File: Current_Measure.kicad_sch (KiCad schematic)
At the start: 4 parts, among them U9401 TMCS1101A2UQDT

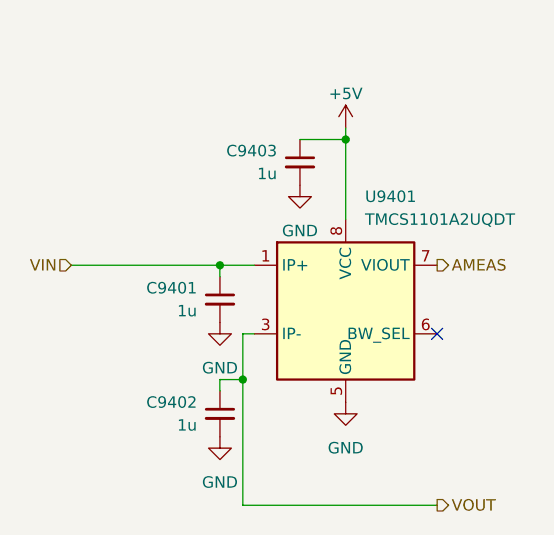
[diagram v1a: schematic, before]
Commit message: wired channel alerts; added schematic for test pbc
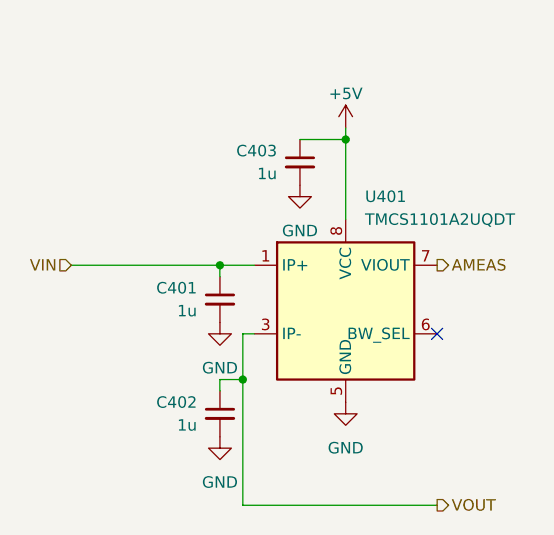
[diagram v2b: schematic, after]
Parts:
- renumbered C9401 to C401, C9402 to C402, C9403 to C403, U9401 to U401
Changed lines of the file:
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@@
 		(on_board yes)
 		(dnp no)
-		(property "Reference" "#PWR09404"
+		(property "Reference" "#PWR0404"
 			(at 157.48 77.47 0)
 			(effects
@@
 		)
 		(instances
+			(project "TEST_PCB"
+				(path "/29496ace-b476-4f24-a65f-9da1dd70122c/504ee284-c5b3-48b9-b988-a6d19662e437"
+					(reference "#PWR01304")
+					(unit 1)
+				)
+				(path "/29496ace-b476-4f24-a65f-9da1dd70122c/02ad1486-0ecd-4655-9f01-754da17b7441/24296571-f4ee-420c-bcfd-9dd9216b9bef"
+					(reference "#PWR0404")
+					(unit 1)
+				)
+			)
 			(project "EPS"
 				(path "/94201994-47b8-4213-8d1a-05da12b2a7b0/48aa2731-b960-4e20-aa69-ef710a76283c"
@@
 		(dnp no)
 		(fields_autoplaced yes)
-		(property "Reference" "#PWR09402"
+		(property "Reference" "#PWR0402"
 			(at 143.51 114.3 0)
 			(effects
@@
 		)
 		(instances
+			(project "TEST_PCB"
+				(path "/29496ace-b476-4f24-a65f-9da1dd70122c/504ee284-c5b3-48b9-b988-a6d19662e437"
+					(reference "#PWR01302")
+					(unit 1)
+				)
+				(path "/29496ace-b476-4f24-a65f-9da1dd70122c/02ad1486-0ecd-4655-9f01-754da17b7441/24296571-f4ee-420c-bcfd-9dd9216b9bef"
+					(reference "#PWR0402")
+					(unit 1)
+				)
+			)
 			(project "EPS"
 				(path "/94201994-47b8-4213-8d1a-05da12b2a7b0/48aa2731-b960-4e20-aa69-ef710a76283c"
@@
 		(on_board yes)
 		(dnp no)
-		(property "Reference" "C9401"
+		(property "Reference" "C401"
 			(at 140.97 91.4462 0)
 			(effects
@@
 		)
 		(instances
+			(project "TEST_PCB"
+				(path "/29496ace-b476-4f24-a65f-9da1dd70122c/504ee284-c5b3-48b9-b988-a6d19662e437"
+					(reference "C1301")
+					(unit 1)
+				)
+				(path "/29496ace-b476-4f24-a65f-9da1dd70122c/02ad1486-0ecd-4655-9f01-754da17b7441/24296571-f4ee-420c-bcfd-9dd9216b9bef"
+					(reference "C401")
+					(unit 1)
+				)
+			)
 			(project "EPS"
 				(path "/94201994-47b8-4213-8d1a-05da12b2a7b0/48aa2731-b960-4e20-aa69-ef710a76283c"
@@
 		(dnp no)
 		(fields_autoplaced yes)
-		(property "Reference" "#PWR09405"
+		(property "Reference" "#PWR0405"
 			(at 157.48 110.49 0)
 			(effects
@@
 		)
 		(instances
+			(project "TEST_PCB"
+				(path "/29496ace-b476-4f24-a65f-9da1dd70122c/504ee284-c5b3-48b9-b988-a6d19662e437"
+					(reference "#PWR01305")
+					(unit 1)
+				)
+				(path "/29496ace-b476-4f24-a65f-9da1dd70122c/02ad1486-0ecd-4655-9f01-754da17b7441/24296571-f4ee-420c-bcfd-9dd9216b9bef"
+					(reference "#PWR0405")
+					(unit 1)
+				)
+			)
 			(project "EPS"
 				(path "/94201994-47b8-4213-8d1a-05da12b2a7b0/48aa2731-b960-4e20-aa69-ef710a76283c"
@@
 		(dnp no)
 		(fields_autoplaced yes)
-		(property "Reference" "U9401"
+		(property "Reference" "U401"
 			(at 159.6233 81.28 0)
 			(effects
@@
 		)
 		(instances
+			(project "TEST_PCB"
+				(path "/29496ace-b476-4f24-a65f-9da1dd70122c/504ee284-c5b3-48b9-b988-a6d19662e437"
+					(reference "U1301")
+					(unit 1)
+				)
+				(path "/29496ace-b476-4f24-a65f-9da1dd70122c/02ad1486-0ecd-4655-9f01-754da17b7441/24296571-f4ee-420c-bcfd-9dd9216b9bef"
+					(reference "U401")
+					(unit 1)
+				)
+			)
 			(project "EPS"
 				(path "/94201994-47b8-4213-8d1a-05da12b2a7b0/48aa2731-b960-4e20-aa69-ef710a76283c"
@@
 		(on_board yes)
 		(dnp no)
-		(property "Reference" "C9403"
+		(property "Reference" "C403"
 			(at 149.86 76.2062 0)
 			(effects
@@
 		)
 		(instances
+			(project "TEST_PCB"
+				(path "/29496ace-b476-4f24-a65f-9da1dd70122c/504ee284-c5b3-48b9-b988-a6d19662e437"
+					(reference "C1303")
+					(unit 1)
+				)
+				(path "/29496ace-b476-4f24-a65f-9da1dd70122c/02ad1486-0ecd-4655-9f01-754da17b7441/24296571-f4ee-420c-bcfd-9dd9216b9bef"
+					(reference "C403")
+					(unit 1)
+				)
+			)
 			(project "EPS"
 				(path "/94201994-47b8-4213-8d1a-05da12b2a7b0/48aa2731-b960-4e20-aa69-ef710a76283c"
@@
 		(on_board yes)
 		(dnp no)
-		(property "Reference" "C9402"
+		(property "Reference" "C402"
 			(at 140.97 104.1462 0)
 			(effects
@@
 		)
 		(instances
+			(project "TEST_PCB"
+				(path "/29496ace-b476-4f24-a65f-9da1dd70122c/504ee284-c5b3-48b9-b988-a6d19662e437"
+					(reference "C1302")
+					(unit 1)
+				)
+				(path "/29496ace-b476-4f24-a65f-9da1dd70122c/02ad1486-0ecd-4655-9f01-754da17b7441/24296571-f4ee-420c-bcfd-9dd9216b9bef"
+					(reference "C402")
+					(unit 1)
+				)
+			)
 			(project "EPS"
 				(path "/94201994-47b8-4213-8d1a-05da12b2a7b0/48aa2731-b960-4e20-aa69-ef710a76283c"
@@
 		(dnp no)
 		(fields_autoplaced yes)
-		(property "Reference" "#PWR09401"
+		(property "Reference" "#PWR0401"
 			(at 143.51 101.6 0)
 			(effects
@@
 		)
 		(instances
+			(project "TEST_PCB"
+				(path "/29496ace-b476-4f24-a65f-9da1dd70122c/504ee284-c5b3-48b9-b988-a6d19662e437"
+					(reference "#PWR01301")
+					(unit 1)
+				)
+				(path "/29496ace-b476-4f24-a65f-9da1dd70122c/02ad1486-0ecd-4655-9f01-754da17b7441/24296571-f4ee-420c-bcfd-9dd9216b9bef"
+					(reference "#PWR0401")
+					(unit 1)
+				)
+			)
 			(project "EPS"
 				(path "/94201994-47b8-4213-8d1a-05da12b2a7b0/48aa2731-b960-4e20-aa69-ef710a76283c"
@@
 		(dnp no)
 		(fields_autoplaced yes)
-		(property "Reference" "#PWR09403"
+		(property "Reference" "#PWR0403"
 			(at 152.4 86.36 0)
 			(effects
@@
 		)
 		(instances
+			(project "TEST_PCB"
+				(path "/29496ace-b476-4f24-a65f-9da1dd70122c/504ee284-c5b3-48b9-b988-a6d19662e437"
+					(reference "#PWR01303")
+					(unit 1)
+				)
+				(path "/29496ace-b476-4f24-a65f-9da1dd70122c/02ad1486-0ecd-4655-9f01-754da17b7441/24296571-f4ee-420c-bcfd-9dd9216b9bef"
+					(reference "#PWR0403")
+					(unit 1)
+				)
+			)
 			(project "EPS"
 				(path "/94201994-47b8-4213-8d1a-05da12b2a7b0/48aa2731-b960-4e20-aa69-ef710a76283c"

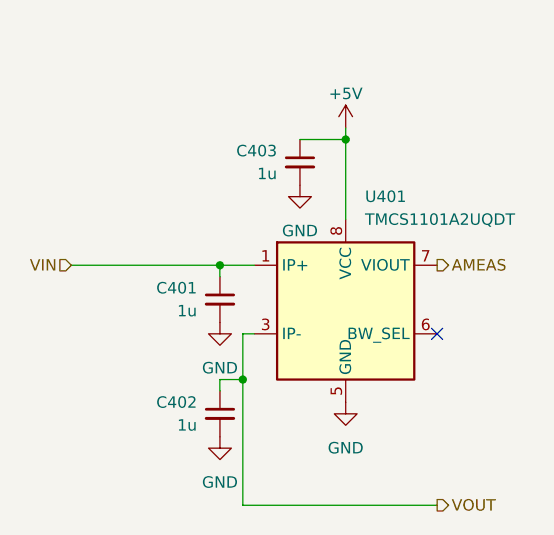
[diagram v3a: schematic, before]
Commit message: added missing heater connectors
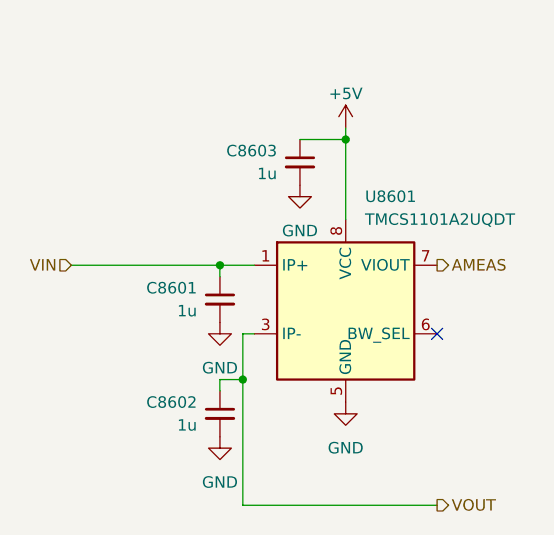
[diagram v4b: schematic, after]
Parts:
- renumbered C401 to C8601, C402 to C8602, C403 to C8603, U401 to U8601
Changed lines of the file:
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@@
 		(on_board yes)
 		(dnp no)
-		(property "Reference" "#PWR0404"
+		(property "Reference" "#PWR08604"
 			(at 157.48 77.47 0)
 			(effects
@@
 		(dnp no)
 		(fields_autoplaced yes)
-		(property "Reference" "#PWR0402"
+		(property "Reference" "#PWR08602"
 			(at 143.51 114.3 0)
 			(effects
@@
 		(on_board yes)
 		(dnp no)
-		(property "Reference" "C401"
+		(property "Reference" "C8601"
 			(at 140.97 91.4462 0)
 			(effects
@@
 		(dnp no)
 		(fields_autoplaced yes)
-		(property "Reference" "#PWR0405"
+		(property "Reference" "#PWR08605"
 			(at 157.48 110.49 0)
 			(effects
@@
 		(dnp no)
 		(fields_autoplaced yes)
-		(property "Reference" "U401"
+		(property "Reference" "U8601"
 			(at 159.6233 81.28 0)
 			(effects
@@
 		(on_board yes)
 		(dnp no)
-		(property "Reference" "C403"
+		(property "Reference" "C8603"
 			(at 149.86 76.2062 0)
 			(effects
@@
 		(on_board yes)
 		(dnp no)
-		(property "Reference" "C402"
+		(property "Reference" "C8602"
 			(at 140.97 104.1462 0)
 			(effects
@@
 		(dnp no)
 		(fields_autoplaced yes)
-		(property "Reference" "#PWR0401"
+		(property "Reference" "#PWR08601"
 			(at 143.51 101.6 0)
 			(effects
@@
 		(dnp no)
 		(fields_autoplaced yes)
-		(property "Reference" "#PWR0403"
+		(property "Reference" "#PWR08603"
 			(at 152.4 86.36 0)
 			(effects

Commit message: restructurization of the entire project improved
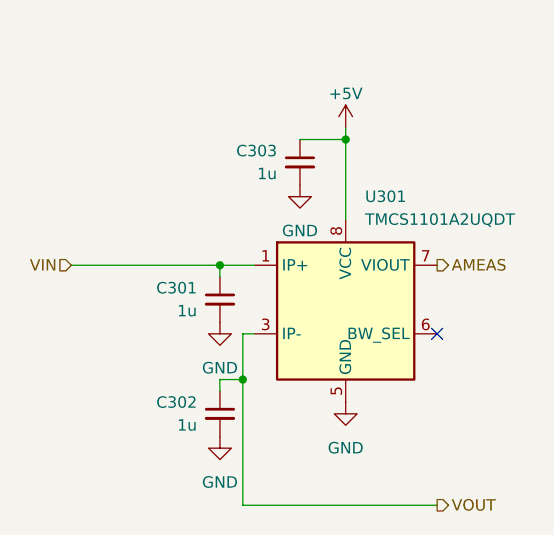
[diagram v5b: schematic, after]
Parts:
- renumbered C8601 to C301, C8602 to C302, C8603 to C303, U8601 to U301

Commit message: added universal switch, added simples current source, reworked test schematic and pcb
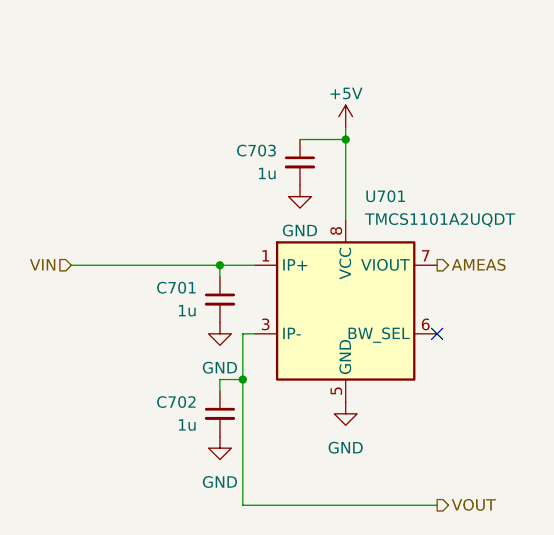
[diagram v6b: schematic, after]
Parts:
- renumbered C301 to C701, C302 to C702, C303 to C703, U301 to U701
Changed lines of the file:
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@@
 		(on_board yes)
 		(dnp no)
-		(property "Reference" "#PWR0304"
+		(property "Reference" "#PWR0704"
 			(at 157.48 77.47 0)
 			(effects
@@
 		)
 		(instances
+			(project "TEST_PCB"
+				(path "/29496ace-b476-4f24-a65f-9da1dd70122c/504ee284-c5b3-48b9-b988-a6d19662e437"
+					(reference "#PWR01404")
+					(unit 1)
+				)
+				(path "/29496ace-b476-4f24-a65f-9da1dd70122c/9ac70773-2304-4605-b1e0-d7d1b5f027ba"
+					(reference "#PWR0704")
+					(unit 1)
+				)
+				(path "/29496ace-b476-4f24-a65f-9da1dd70122c/02ad1486-0ecd-4655-9f01-754da17b7441/24296571-f4ee-420c-bcfd-9dd9216b9bef"
+					(reference "#PWR01604")
+					(unit 1)
+				)
+			)
 			(project "EPS_CORE"
 				(path "/43e5e7c8-e7e0-4528-9a3e-b1557849918d/136d551b-dd5b-42cc-aebd-902cdeeb5d77"
@@
 		(dnp no)
 		(fields_autoplaced yes)
-		(property "Reference" "#PWR0302"
+		(property "Reference" "#PWR0702"
 			(at 143.51 114.3 0)
 			(effects
@@
 		)
 		(instances
+			(project "TEST_PCB"
+				(path "/29496ace-b476-4f24-a65f-9da1dd70122c/504ee284-c5b3-48b9-b988-a6d19662e437"
+					(reference "#PWR01402")
+					(unit 1)
+				)
+				(path "/29496ace-b476-4f24-a65f-9da1dd70122c/9ac70773-2304-4605-b1e0-d7d1b5f027ba"
+					(reference "#PWR0702")
+					(unit 1)
+				)
+				(path "/29496ace-b476-4f24-a65f-9da1dd70122c/02ad1486-0ecd-4655-9f01-754da17b7441/24296571-f4ee-420c-bcfd-9dd9216b9bef"
+					(reference "#PWR01602")
+					(unit 1)
+				)
+			)
 			(project "EPS_CORE"
 				(path "/43e5e7c8-e7e0-4528-9a3e-b1557849918d/136d551b-dd5b-42cc-aebd-902cdeeb5d77"
@@
 		(on_board yes)
 		(dnp no)
-		(property "Reference" "C301"
+		(property "Reference" "C701"
 			(at 140.97 91.4462 0)
 			(effects
@@
 		)
 		(instances
+			(project "TEST_PCB"
+				(path "/29496ace-b476-4f24-a65f-9da1dd70122c/504ee284-c5b3-48b9-b988-a6d19662e437"
+					(reference "C1401")
+					(unit 1)
+				)
+				(path "/29496ace-b476-4f24-a65f-9da1dd70122c/9ac70773-2304-4605-b1e0-d7d1b5f027ba"
+					(reference "C701")
+					(unit 1)
+				)
+				(path "/29496ace-b476-4f24-a65f-9da1dd70122c/02ad1486-0ecd-4655-9f01-754da17b7441/24296571-f4ee-420c-bcfd-9dd9216b9bef"
+					(reference "C1601")
+					(unit 1)
+				)
+			)
 			(project "EPS_CORE"
 				(path "/43e5e7c8-e7e0-4528-9a3e-b1557849918d/136d551b-dd5b-42cc-aebd-902cdeeb5d77"
@@
 		(dnp no)
 		(fields_autoplaced yes)
-		(property "Reference" "#PWR0305"
+		(property "Reference" "#PWR0705"
 			(at 157.48 110.49 0)
 			(effects
@@
 		)
 		(instances
+			(project "TEST_PCB"
+				(path "/29496ace-b476-4f24-a65f-9da1dd70122c/504ee284-c5b3-48b9-b988-a6d19662e437"
+					(reference "#PWR01405")
+					(unit 1)
+				)
+				(path "/29496ace-b476-4f24-a65f-9da1dd70122c/9ac70773-2304-4605-b1e0-d7d1b5f027ba"
+					(reference "#PWR0705")
+					(unit 1)
+				)
+				(path "/29496ace-b476-4f24-a65f-9da1dd70122c/02ad1486-0ecd-4655-9f01-754da17b7441/24296571-f4ee-420c-bcfd-9dd9216b9bef"
+					(reference "#PWR01605")
+					(unit 1)
+				)
+			)
 			(project "EPS_CORE"
 				(path "/43e5e7c8-e7e0-4528-9a3e-b1557849918d/136d551b-dd5b-42cc-aebd-902cdeeb5d77"
@@
 		(dnp no)
 		(fields_autoplaced yes)
-		(property "Reference" "U301"
+		(property "Reference" "U701"
 			(at 159.6233 81.28 0)
 			(effects
@@
 		)
 		(instances
+			(project "TEST_PCB"
+				(path "/29496ace-b476-4f24-a65f-9da1dd70122c/504ee284-c5b3-48b9-b988-a6d19662e437"
+					(reference "U1401")
+					(unit 1)
+				)
+				(path "/29496ace-b476-4f24-a65f-9da1dd70122c/9ac70773-2304-4605-b1e0-d7d1b5f027ba"
+					(reference "U701")
+					(unit 1)
+				)
+				(path "/29496ace-b476-4f24-a65f-9da1dd70122c/02ad1486-0ecd-4655-9f01-754da17b7441/24296571-f4ee-420c-bcfd-9dd9216b9bef"
+					(reference "U1601")
+					(unit 1)
+				)
+			)
 			(project "EPS_CORE"
 				(path "/43e5e7c8-e7e0-4528-9a3e-b1557849918d/136d551b-dd5b-42cc-aebd-902cdeeb5d77"
@@
 		(on_board yes)
 		(dnp no)
-		(property "Reference" "C303"
+		(property "Reference" "C703"
 			(at 149.86 76.2062 0)
 			(effects
@@
 		)
 		(instances
+			(project "TEST_PCB"
+				(path "/29496ace-b476-4f24-a65f-9da1dd70122c/504ee284-c5b3-48b9-b988-a6d19662e437"
+					(reference "C1403")
+					(unit 1)
+				)
+				(path "/29496ace-b476-4f24-a65f-9da1dd70122c/9ac70773-2304-4605-b1e0-d7d1b5f027ba"
+					(reference "C703")
+					(unit 1)
+				)
+				(path "/29496ace-b476-4f24-a65f-9da1dd70122c/02ad1486-0ecd-4655-9f01-754da17b7441/24296571-f4ee-420c-bcfd-9dd9216b9bef"
+					(reference "C1603")
+					(unit 1)
+				)
+			)
 			(project "EPS_CORE"
 				(path "/43e5e7c8-e7e0-4528-9a3e-b1557849918d/136d551b-dd5b-42cc-aebd-902cdeeb5d77"
@@
 		(on_board yes)
 		(dnp no)
-		(property "Reference" "C302"
+		(property "Reference" "C702"
 			(at 140.97 104.1462 0)
 			(effects
@@
 		)
 		(instances
+			(project "TEST_PCB"
+				(path "/29496ace-b476-4f24-a65f-9da1dd70122c/504ee284-c5b3-48b9-b988-a6d19662e437"
+					(reference "C1402")
+					(unit 1)
+				)
+				(path "/29496ace-b476-4f24-a65f-9da1dd70122c/9ac70773-2304-4605-b1e0-d7d1b5f027ba"
+					(reference "C702")
+					(unit 1)
+				)
+				(path "/29496ace-b476-4f24-a65f-9da1dd70122c/02ad1486-0ecd-4655-9f01-754da17b7441/24296571-f4ee-420c-bcfd-9dd9216b9bef"
+					(reference "C1602")
+					(unit 1)
+				)
+			)
 			(project "EPS_CORE"
 				(path "/43e5e7c8-e7e0-4528-9a3e-b1557849918d/136d551b-dd5b-42cc-aebd-902cdeeb5d77"
@@
 		(dnp no)
 		(fields_autoplaced yes)
-		(property "Reference" "#PWR0301"
+		(property "Reference" "#PWR0701"
 			(at 143.51 101.6 0)
 			(effects
@@
 		)
 		(instances
+			(project "TEST_PCB"
+				(path "/29496ace-b476-4f24-a65f-9da1dd70122c/504ee284-c5b3-48b9-b988-a6d19662e437"
+					(reference "#PWR01401")
+					(unit 1)
+				)
+				(path "/29496ace-b476-4f24-a65f-9da1dd70122c/9ac70773-2304-4605-b1e0-d7d1b5f027ba"
+					(reference "#PWR0701")
+					(unit 1)
+				)
+				(path "/29496ace-b476-4f24-a65f-9da1dd70122c/02ad1486-0ecd-4655-9f01-754da17b7441/24296571-f4ee-420c-bcfd-9dd9216b9bef"
+					(reference "#PWR01601")
+					(unit 1)
+				)
+			)
 			(project "EPS_CORE"
 				(path "/43e5e7c8-e7e0-4528-9a3e-b1557849918d/136d551b-dd5b-42cc-aebd-902cdeeb5d77"
@@
 		(dnp no)
 		(fields_autoplaced yes)
-		(property "Reference" "#PWR0303"
+		(property "Reference" "#PWR0703"
 			(at 152.4 86.36 0)
 			(effects
@@
 		)
 		(instances
+			(project "TEST_PCB"
+				(path "/29496ace-b476-4f24-a65f-9da1dd70122c/504ee284-c5b3-48b9-b988-a6d19662e437"
+					(reference "#PWR01403")
+					(unit 1)
+				)
+				(path "/29496ace-b476-4f24-a65f-9da1dd70122c/9ac70773-2304-4605-b1e0-d7d1b5f027ba"
+					(reference "#PWR0703")
+					(unit 1)
+				)
+				(path "/29496ace-b476-4f24-a65f-9da1dd70122c/02ad1486-0ecd-4655-9f01-754da17b7441/24296571-f4ee-420c-bcfd-9dd9216b9bef"
+					(reference "#PWR01603")
+					(unit 1)
+				)
+			)
 			(project "EPS_CORE"
 				(path "/43e5e7c8-e7e0-4528-9a3e-b1557849918d/136d551b-dd5b-42cc-aebd-902cdeeb5d77"

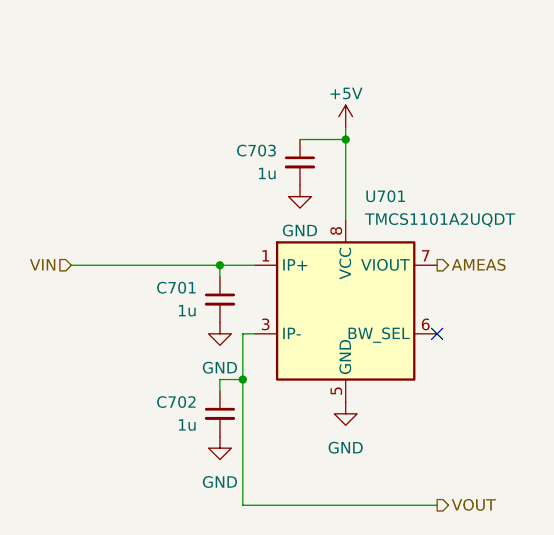
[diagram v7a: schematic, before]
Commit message: changes based on test board manufacturing, mostly added voltage dividers
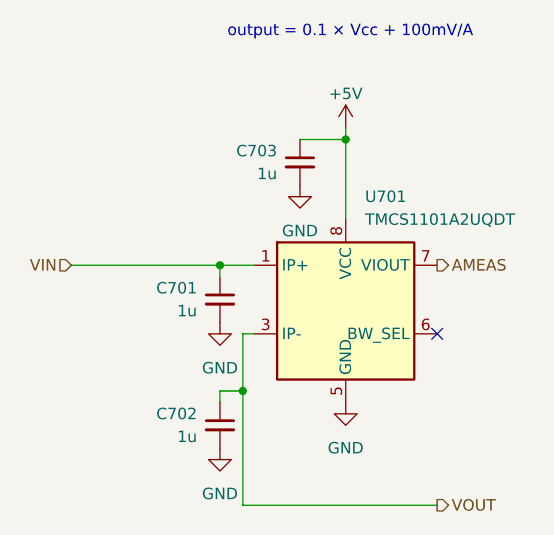
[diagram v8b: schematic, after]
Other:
- note added: "output = 0.1 × Vcc + 100mV/A"
- moved on the sheet: C702
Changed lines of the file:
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@@
 	(generator_version "9.0")
 	(paper "A4")
-	(junction
-		(at 146.05 101.6)
-		(diameter 0)
-		(color 0 0 0 0)
+	(text "output = 0.1 × Vcc + 100mV/A\n"
+		(exclude_from_sim no)
+		(at 157.988 62.992 0)
+		(effects
+			(font
+				(size 1.27 1.27)
+			)
+		)
 	)
 	(junction
@@
 	)
 	(junction
+		(at 146.05 102.87)
+		(diameter 0)
+		(color 0 0 0 0)
+	)
+	(junction
 		(at 143.51 88.9)
 		(diameter 0)
@@
 	(wire
 		(pts
-			(xy 143.51 101.6) (xy 143.51 102.87)
+			(xy 143.51 102.87) (xy 143.51 104.14)
 		)
 		(stroke
@@
 	(wire
 		(pts
-			(xy 146.05 101.6) (xy 146.05 115.57)
+			(xy 146.05 102.87) (xy 146.05 115.57)
 		)
 		(stroke
@@
 	(wire
 		(pts
-			(xy 143.51 101.6) (xy 146.05 101.6)
+			(xy 143.51 102.87) (xy 146.05 102.87)
 		)
 		(stroke
@@
 	(wire
 		(pts
-			(xy 146.05 96.52) (xy 146.05 101.6)
+			(xy 157.48 83.82) (xy 157.48 74.93)
 		)
 		(stroke
@@
 	(wire
 		(pts
-			(xy 157.48 83.82) (xy 157.48 74.93)
+			(xy 157.48 74.93) (xy 152.4 74.93)
 		)
 		(stroke
@@
 	(wire
 		(pts
-			(xy 157.48 74.93) (xy 152.4 74.93)
+			(xy 143.51 88.9) (xy 147.32 88.9)
 		)
 		(stroke
@@
 	(wire
 		(pts
-			(xy 143.51 88.9) (xy 147.32 88.9)
+			(xy 146.05 96.52) (xy 146.05 102.87)
 		)
 		(stroke
@@
 	(symbol
 		(lib_id "power:GND")
-		(at 143.51 107.95 0)
+		(at 143.51 109.22 0)
 		(unit 1)
 		(exclude_from_sim no)
@@
 		(fields_autoplaced yes)
 		(property "Reference" "#PWR0702"
+			(at 143.51 115.57 0)
+			(effects
+				(font
+					(size 1.27 1.27)
+				)
+				(hide yes)
+			)
+		)
+		(property "Value" "GND"
 			(at 143.51 114.3 0)
 			(effects
@@
 					(size 1.27 1.27)
 				)
-				(hide yes)
-			)
-		)
-		(property "Value" "GND"
-			(at 143.51 113.03 0)
-			(effects
-				(font
-					(size 1.27 1.27)
-				)
 			)
 		)
 		(property "Footprint" ""
-			(at 143.51 107.95 0)
+			(at 143.51 109.22 0)
 			(effects
 				(font
@@
 		)
 		(property "Datasheet" ""
-			(at 143.51 107.95 0)
+			(at 143.51 109.22 0)
 			(effects
 				(font
@@
 		)
 		(property "Description" "Power symbol creates a global label with name \"GND\" , ground"
-			(at 143.51 107.95 0)
+			(at 143.51 109.22 0)
 			(effects
 				(font
@@
 	(symbol
 		(lib_id "Device:C_Small")
-		(at 143.51 105.41 0)
+		(at 143.51 106.68 0)
 		(mirror y)
 		(unit 1)
@@
 		(dnp no)
 		(property "Reference" "C702"
-			(at 140.97 104.1462 0)
+			(at 140.97 105.4162 0)
 			(effects
 				(font
@@
 		)
 		(property "Value" "1u"
-			(at 140.97 106.6862 0)
+			(at 140.97 107.9562 0)
 			(effects
 				(font
@@
 		)
 		(property "Footprint" "Capacitor_SMD:C_0603_1608Metric_Pad1.08x0.95mm_HandSolder"
-			(at 143.51 105.41 0)
+			(at 143.51 106.68 0)
 			(effects
 				(font
@@
 		)
 		(property "Datasheet" "~"
-			(at 143.51 105.41 0)
+			(at 143.51 106.68 0)
 			(effects
 				(font
@@
 		)
 		(property "Description" "Unpolarized capacitor, small symbol"
-			(at 143.51 105.41 0)
+			(at 143.51 106.68 0)
 			(effects
 				(font
@@
 		)
 		(property "CONFIG" ""
-			(at 143.51 105.41 0)
+			(at 143.51 106.68 0)
 			(effects
 				(font
@@
 		)
 		(property "Specification" ""
-			(at 143.51 105.41 0)
+			(at 143.51 106.68 0)
 			(effects
 				(font
@@
 		)
 		(property "mouser_pn" ""
-			(at 143.51 105.41 0)
-			(effects
-				(font
+			(at 143.51 106.68 0)
+			(effects
+				(font
